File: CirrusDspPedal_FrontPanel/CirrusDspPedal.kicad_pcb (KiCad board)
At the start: 2 copper layers, 112.5 x 86.4 mm, 5 parts

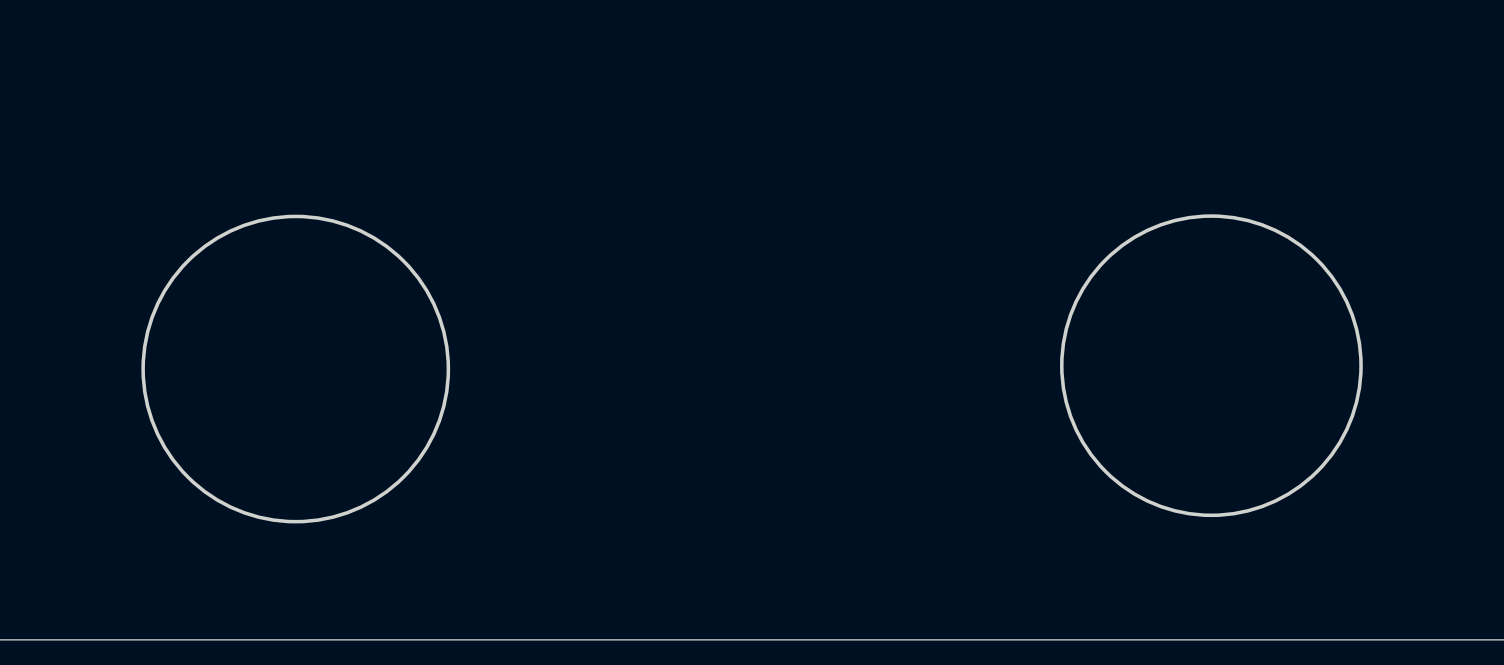
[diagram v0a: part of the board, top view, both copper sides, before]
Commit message: modified front panel
Raised footswitch holes by 3mm
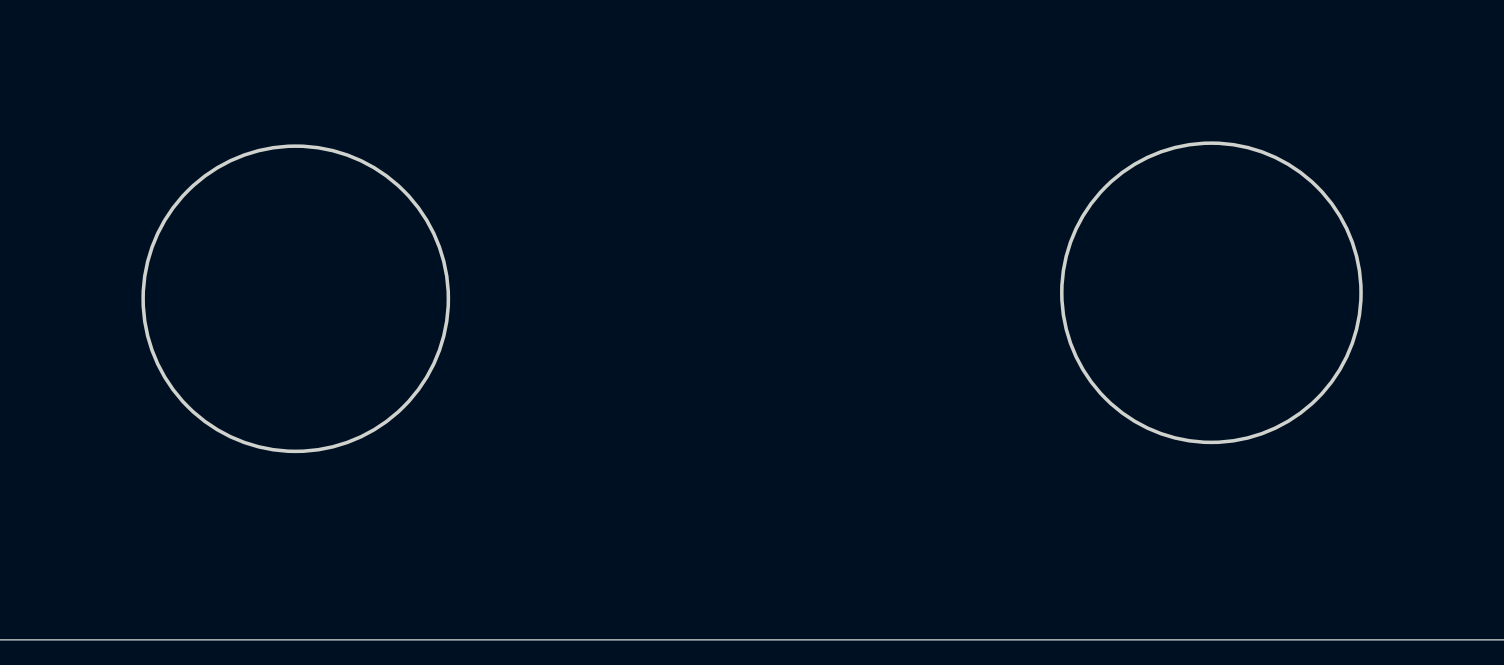
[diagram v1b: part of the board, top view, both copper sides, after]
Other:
- outline, holes or cut-outs redrawn
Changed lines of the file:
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@@
-(kicad_pcb (version 20171130) (host pcbnew 5.1.8-db9833491~87~ubuntu18.04.1)
+(kicad_pcb (version 20171130) (host pcbnew "(5.1.8-0-10_14)")
   (general
     (thickness 1.6)
@@
     (pad_to_mask_clearance 0)
     (aux_axis_origin 0 0)
-    (grid_origin 196.469 127.254)
+    (grid_origin 148.463 94.615)
     (visible_elements FFFFFF7F)
     (pcbplotparams
@@
       (effects (font (size 1 1) (thickness 0.15)))
     )
-    (fp_text user %R (at 0.3 0) (layer F.Fab)
-      (effects (font (size 1 1) (thickness 0.15)))
-    )
-    (fp_circle (center 0 0) (end 4 0) (layer Cmts.User) (width 0.15))
-    (fp_circle (center 0 0) (end 4.25 0) (layer F.CrtYd) (width 0.05))
+    (fp_circle (center 0 0) (end 4 0) (layer Cmts.User) (width 0.15))
+    (fp_circle (center 0 0) (end 4.25 0) (layer F.CrtYd) (width 0.05))
+    (fp_text user %R (at 0.3 0) (layer F.Fab)
+      (effects (font (size 1 1) (thickness 0.15)))
+    )
     (pad 1 thru_hole circle (at 0 0) (size 8 8) (drill 4) (layers *.Cu *.Mask))
   )
@@
       (effects (font (size 1 1) (thickness 0.15)))
     )
-    (fp_text user %R (at 0.3 0) (layer F.Fab)
-      (effects (font (size 1 1) (thickness 0.15)))
-    )
-    (fp_circle (center 0 0) (end 4 0) (layer Cmts.User) (width 0.15))
-    (fp_circle (center 0 0) (end 4.25 0) (layer F.CrtYd) (width 0.05))
+    (fp_circle (center 0 0) (end 4 0) (layer Cmts.User) (width 0.15))
+    (fp_circle (center 0 0) (end 4.25 0) (layer F.CrtYd) (width 0.05))
+    (fp_text user %R (at 0.3 0) (layer F.Fab)
+      (effects (font (size 1 1) (thickness 0.15)))
+    )
     (pad 1 thru_hole circle (at 0 0) (size 8 8) (drill 4) (layers *.Cu *.Mask))
   )
@@
       (effects (font (size 1 1) (thickness 0.15)))
     )
-    (fp_text user %R (at 0.3 0) (layer F.Fab)
-      (effects (font (size 1 1) (thickness 0.15)))
-    )
-    (fp_circle (center 0 0) (end 4 0) (layer Cmts.User) (width 0.15))
-    (fp_circle (center 0 0) (end 4.25 0) (layer F.CrtYd) (width 0.05))
+    (fp_circle (center 0 0) (end 4 0) (layer Cmts.User) (width 0.15))
+    (fp_circle (center 0 0) (end 4.25 0) (layer F.CrtYd) (width 0.05))
+    (fp_text user %R (at 0.3 0) (layer F.Fab)
+      (effects (font (size 1 1) (thickness 0.15)))
+    )
     (pad 1 thru_hole circle (at 0 0) (size 8 8) (drill 4) (layers *.Cu *.Mask))
   )
@@
       (effects (font (size 1 1) (thickness 0.15)))
     )
-    (fp_text user %R (at 0.3 0) (layer F.Fab)
-      (effects (font (size 1 1) (thickness 0.15)))
-    )
-    (fp_circle (center 0 0) (end 4 0) (layer Cmts.User) (width 0.15))
-    (fp_circle (center 0 0) (end 4.25 0) (layer F.CrtYd) (width 0.05))
+    (fp_circle (center 0 0) (end 4 0) (layer Cmts.User) (width 0.15))
+    (fp_circle (center 0 0) (end 4.25 0) (layer F.CrtYd) (width 0.05))
+    (fp_text user %R (at 0.3 0) (layer F.Fab)
+      (effects (font (size 1 1) (thickness 0.15)))
+    )
     (pad 1 thru_hole circle (at 0 0) (size 8 8) (drill 4) (layers *.Cu *.Mask))
   )
@@
   (gr_line (start 100.33 78.232) (end 97.536 78.232) (layer F.SilkS) (width 0.12))
   (gr_circle (center 100.33 78.232) (end 100.33 78.232) (layer F.SilkS) (width 2))
-  (gr_circle (center 129.286 129.4765) (end 135.763042 129.4765) (layer Edge.Cuts) (width 0.15))
+  (gr_circle (center 129.286 126.492) (end 135.763042 126.492) (layer Edge.Cuts) (width 0.15))
   (gr_line (start 171.323 123.317) (end 172.820876 121.713532) (layer Dwgs.User) (width 0.15))
   (gr_line (start 122.555 105.513799) (end 136.012121 105.513799) (layer Dwgs.User) (width 0.15))
@@
   (gr_line (start 122.555 136.271) (end 122.555 105.513799) (layer Dwgs.User) (width 0.15))
   (gr_line (start 136.012121 136.271) (end 122.555 136.271) (layer Dwgs.User) (width 0.15))
-  (gr_circle (center 168.148 129.333532) (end 174.498 129.333532) (layer Edge.Cuts) (width 0.15))
+  (gr_circle (center 168.148 126.238) (end 174.498 126.238) (layer Edge.Cuts) (width 0.15))
   (gr_line (start 98.425 55.1815) (end 99.06 54.5465) (layer Edge.Cuts) (width 0.05))
   (gr_line (start 98.425 60.325) (end 98.425 55.1815) (layer Edge.Cuts) (width 0.05))
@@
     (connect_pads yes (clearance 0.508))
     (min_thickness 0.254)
-    (fill yes (arc_segments 32) (thermal_gap 0.508) (thermal_bridge_width 0.508))
+    (fill (arc_segments 32) (thermal_gap 0.508) (thermal_bridge_width 0.508))
     (polygon
       (pts
